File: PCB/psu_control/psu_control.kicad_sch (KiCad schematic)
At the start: 7 parts, among them Q1 SSM3J372R, U1 LM810M3-4.63, U2 Teensy_LC

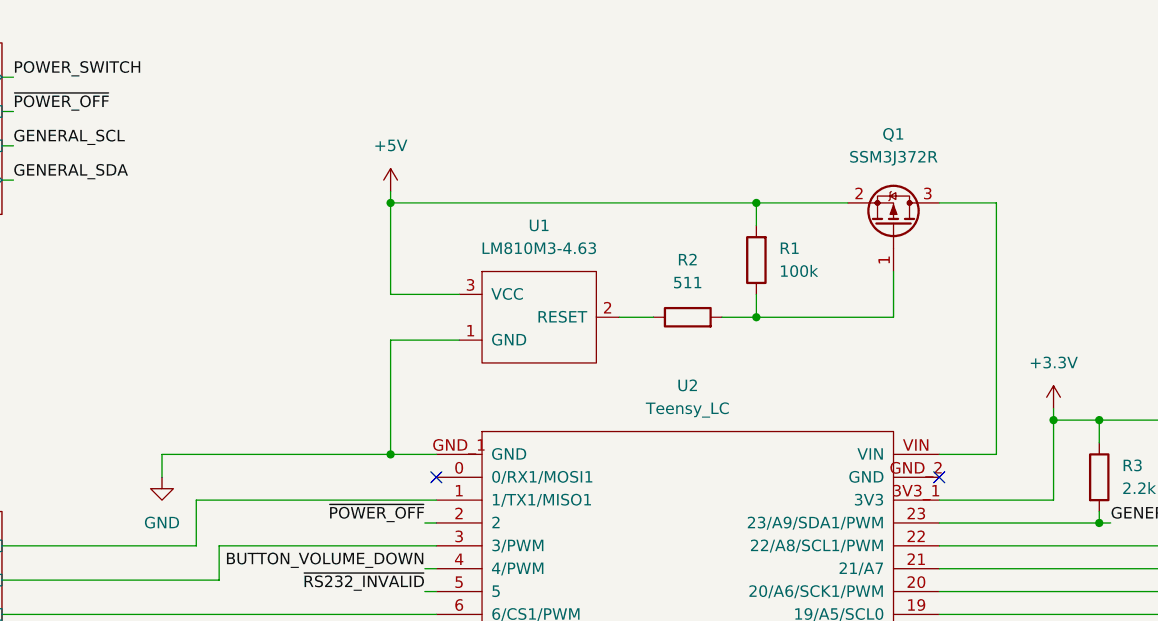
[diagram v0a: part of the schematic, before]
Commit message: Remove voltage supervisors
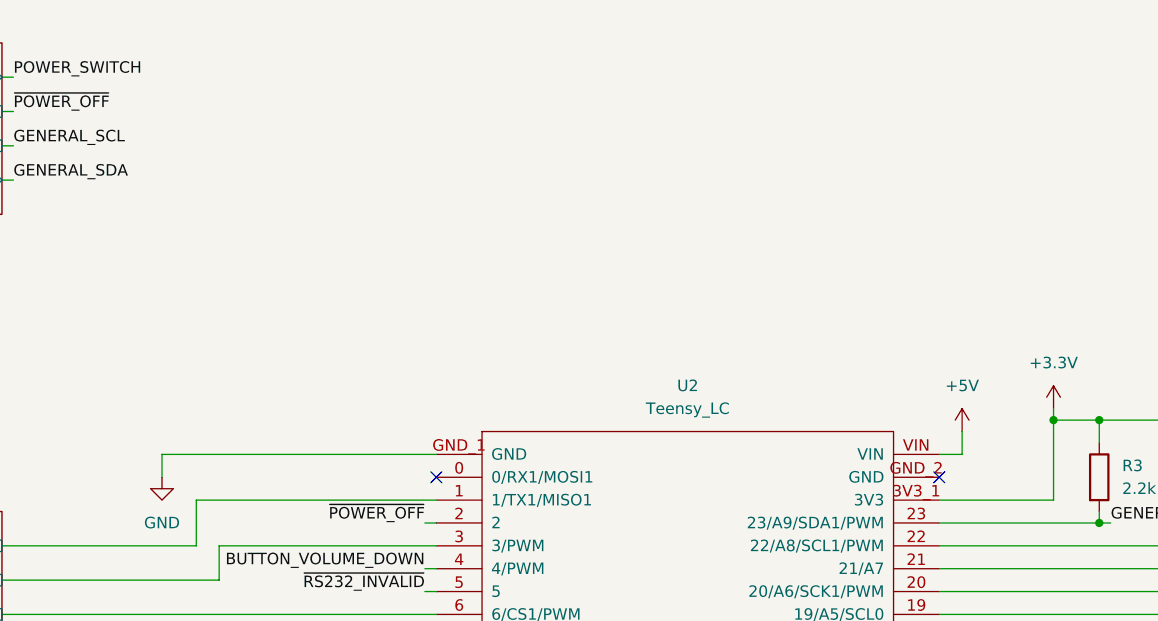
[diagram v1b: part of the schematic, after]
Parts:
- removed Q1: SSM3J372R, Package_TO_SOT_SMD:SOT-23, symbol Device:Q_PMOS_GSD
- removed R1: 100k, Resistor_SMD:R_0805_2012Metric, symbol Device:R
- removed R2: 511, Resistor_SMD:R_0805_2012Metric, symbol Device:R
- removed U1: LM810M3-4.63, Package_TO_SOT_SMD:SOT-23, symbol t-top:LM810
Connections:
- net +5V: now also U2.VIN
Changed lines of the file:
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@@
   (junction (at 168.91 69.85) (diameter 0) (color 0 0 0 0)
   )
-  (junction (at 95.25 45.72) (diameter 0) (color 0 0 0 0)
-  )
-  (junction (at 135.89 45.72) (diameter 0) (color 0 0 0 0)
-  )
-  (junction (at 95.25 73.66) (diameter 0) (color 0 0 0 0)
-  )
   (junction (at 190.5 83.82) (diameter 0) (color 0 0 0 0)
-  )
-  (junction (at 135.89 58.42) (diameter 0) (color 0 0 0 0)
   )
   (junction (at 173.99 69.85) (diameter 0) (color 0 0 0 0)
@@
     (stroke (width 0) (type default) (color 0 0 0 0))
   )
-  (wire (pts (xy 162.56 73.66) (xy 156.21 73.66))
-    (stroke (width 0) (type default) (color 0 0 0 0))
-  )
   (wire (pts (xy 74.93 96.52) (xy 74.93 118.11))
     (stroke (width 0) (type default) (color 0 0 0 0))
@@
     (stroke (width 0) (type default) (color 0 0 0 0))
   )
-  (wire (pts (xy 120.65 58.42) (xy 124.46 58.42))
-    (stroke (width 0) (type default) (color 0 0 0 0))
-  )
-  (wire (pts (xy 95.25 60.96) (xy 95.25 73.66))
-    (stroke (width 0) (type default) (color 0 0 0 0))
-  )
-  (wire (pts (xy 135.89 58.42) (xy 135.89 55.88))
-    (stroke (width 0) (type default) (color 0 0 0 0))
-  )
   (wire (pts (xy 168.91 68.58) (xy 168.91 69.85))
     (stroke (width 0) (type default) (color 0 0 0 0))
   )
+  (wire (pts (xy 158.75 71.12) (xy 158.75 73.66))
+    (stroke (width 0) (type default) (color 0 0 0 0))
+  )
   (wire (pts (xy 212.09 147.32) (xy 213.36 147.32))
     (stroke (width 0) (type default) (color 0 0 0 0))
@@
     (stroke (width 0) (type default) (color 0 0 0 0))
   )
-  (wire (pts (xy 95.25 55.88) (xy 102.87 55.88))
-    (stroke (width 0) (type default) (color 0 0 0 0))
-  )
   (wire (pts (xy 156.21 78.74) (xy 168.91 78.74))
     (stroke (width 0) (type default) (color 0 0 0 0))
@@
     (stroke (width 0) (type default) (color 0 0 0 0))
   )
-  (wire (pts (xy 135.89 45.72) (xy 135.89 48.26))
+  (wire (pts (xy 158.75 73.66) (xy 156.21 73.66))
     (stroke (width 0) (type default) (color 0 0 0 0))
   )
@@
     (stroke (width 0) (type default) (color 0 0 0 0))
   )
-  (wire (pts (xy 151.13 53.34) (xy 151.13 58.42))
-    (stroke (width 0) (type default) (color 0 0 0 0))
-  )
   (wire (pts (xy 156.21 91.44) (xy 210.82 91.44))
     (stroke (width 0) (type default) (color 0 0 0 0))
@@
     (stroke (width 0) (type default) (color 0 0 0 0))
   )
-  (wire (pts (xy 100.33 73.66) (xy 95.25 73.66))
-    (stroke (width 0) (type default) (color 0 0 0 0))
-  )
   (wire (pts (xy 185.42 129.54) (xy 185.42 104.14))
     (stroke (width 0) (type default) (color 0 0 0 0))
@@
     (stroke (width 0) (type default) (color 0 0 0 0))
   )
-  (wire (pts (xy 135.89 45.72) (xy 146.05 45.72))
-    (stroke (width 0) (type default) (color 0 0 0 0))
-  )
   (wire (pts (xy 190.5 69.85) (xy 190.5 72.39))
     (stroke (width 0) (type default) (color 0 0 0 0))
   )
-  (wire (pts (xy 132.08 58.42) (xy 135.89 58.42))
-    (stroke (width 0) (type default) (color 0 0 0 0))
-  )
   (wire (pts (xy 212.09 143.51) (xy 213.36 143.51))
     (stroke (width 0) (type default) (color 0 0 0 0))
   )
-  (wire (pts (xy 95.25 45.72) (xy 95.25 55.88))
-    (stroke (width 0) (type default) (color 0 0 0 0))
-  )
   (wire (pts (xy 156.21 101.6) (xy 186.69 101.6))
     (stroke (width 0) (type default) (color 0 0 0 0))
@@
     (stroke (width 0) (type default) (color 0 0 0 0))
   )
-  (wire (pts (xy 162.56 45.72) (xy 162.56 73.66))
-    (stroke (width 0) (type default) (color 0 0 0 0))
-  )
   (wire (pts (xy 99.06 99.06) (xy 100.33 99.06))
     (stroke (width 0) (type default) (color 0 0 0 0))
   )
-  (wire (pts (xy 69.85 73.66) (xy 95.25 73.66))
+  (wire (pts (xy 69.85 73.66) (xy 100.33 73.66))
     (stroke (width 0) (type default) (color 0 0 0 0))
   )
@@
     (stroke (width 0) (type default) (color 0 0 0 0))
   )
-  (wire (pts (xy 95.25 45.72) (xy 135.89 45.72))
-    (stroke (width 0) (type default) (color 0 0 0 0))
-  )
   (wire (pts (xy 156.21 96.52) (xy 189.23 96.52))
     (stroke (width 0) (type default) (color 0 0 0 0))
   )
-  (wire (pts (xy 151.13 58.42) (xy 135.89 58.42))
-    (stroke (width 0) (type default) (color 0 0 0 0))
-  )
   (wire (pts (xy 52.07 121.92) (xy 53.34 121.92))
     (stroke (width 0) (type default) (color 0 0 0 0))
@@
     (stroke (width 0) (type default) (color 0 0 0 0))
   )
-  (wire (pts (xy 156.21 45.72) (xy 162.56 45.72))
-    (stroke (width 0) (type default) (color 0 0 0 0))
-  )
   (wire (pts (xy 212.09 111.76) (xy 213.36 111.76))
     (stroke (width 0) (type default) (color 0 0 0 0))
@@
     (stroke (width 0) (type default) (color 0 0 0 0))
   )
-  (wire (pts (xy 95.25 44.45) (xy 95.25 45.72))
-    (stroke (width 0) (type default) (color 0 0 0 0))
-  )
   (wire (pts (xy 74.93 118.11) (xy 52.07 118.11))
     (stroke (width 0) (type default) (color 0 0 0 0))
@@
   )
   (wire (pts (xy 76.2 83.82) (xy 100.33 83.82))
-    (stroke (width 0) (type default) (color 0 0 0 0))
-  )
-  (wire (pts (xy 102.87 60.96) (xy 95.25 60.96))
     (stroke (width 0) (type default) (color 0 0 0 0))
   )
@@
     (pin "1")
   )
-  (symbol (lib_id "t-top:LM810") (at 111.76 52.07 0) (unit 1)
+  (symbol (lib_id "power:+5V") (at 158.75 71.12 0) (unit 1)
     (in_bom yes) (on_board yes) (fields_autoplaced)
-    (property "Reference" "U1" (id 0) (at 111.76 48.26 0))
-    (property "Value" "LM810M3-4.63" (id 1) (at 111.76 50.8 0))
-    (property "Footprint" "Package_TO_SOT_SMD:SOT-23" (id 2) (at 111.76 52.07 0)
-      (effects (font (size 1.27 1.27)) hide)
-    )
-    (property "Datasheet" "" (id 3) (at 111.76 52.07 0)
-      (effects (font (size 1.27 1.27)) hide)
-    )
-    (pin "1")
-    (pin "2")
-    (pin "3")
-  )
-  (symbol (lib_id "Device:Q_PMOS_GSD") (at 151.13 48.26 270) (mirror x) (unit 1)
-    (in_bom yes) (on_board yes) (fields_autoplaced)
-    (property "Reference" "Q1" (id 0) (at 151.13 38.1 90))
-    (property "Value" "SSM3J372R" (id 1) (at 151.13 40.64 90))
-    (property "Footprint" "Package_TO_SOT_SMD:SOT-23" (id 2) (at 153.67 43.18 0)
-      (effects (font (size 1.27 1.27)) hide)
-    )
-    (property "Datasheet" "~" (id 3) (at 151.13 48.26 0)
-      (effects (font (size 1.27 1.27)) hide)
-    )
-    (pin "1")
-    (pin "2")
-    (pin "3")
-  )
-  (symbol (lib_id "Device:R") (at 135.89 52.07 180) (unit 1)
-    (in_bom yes) (on_board yes) (fields_autoplaced)
-    (property "Reference" "R1" (id 0) (at 138.43 50.7999 0)
-      (effects (font (size 1.27 1.27)) (justify right))
-    )
-    (property "Value" "100k" (id 1) (at 138.43 53.3399 0)
-      (effects (font (size 1.27 1.27)) (justify right))
-    )
-    (property "Footprint" "Resistor_SMD:R_0805_2012Metric" (id 2) (at 137.668 52.07 90)
-      (effects (font (size 1.27 1.27)) hide)
-    )
-    (property "Datasheet" "~" (id 3) (at 135.89 52.07 0)
-      (effects (font (size 1.27 1.27)) hide)
-    )
-    (pin "1")
-    (pin "2")
-  )
-  (symbol (lib_id "power:+5V") (at 95.25 44.45 0) (unit 1)
-    (in_bom yes) (on_board yes) (fields_autoplaced)
-    (property "Reference" "#PWR0103" (id 0) (at 95.25 48.26 0)
-      (effects (font (size 1.27 1.27)) hide)
-    )
-    (property "Value" "+5V" (id 1) (at 95.25 39.37 0))
-    (property "Footprint" "" (id 2) (at 95.25 44.45 0)
-      (effects (font (size 1.27 1.27)) hide)
-    )
-    (property "Datasheet" "" (id 3) (at 95.25 44.45 0)
+    (property "Reference" "#PWR0103" (id 0) (at 158.75 74.93 0)
+      (effects (font (size 1.27 1.27)) hide)
+    )
+    (property "Value" "+5V" (id 1) (at 158.75 66.04 0))
+    (property "Footprint" "" (id 2) (at 158.75 71.12 0)
+      (effects (font (size 1.27 1.27)) hide)
+    )
+    (property "Datasheet" "" (id 3) (at 158.75 71.12 0)
       (effects (font (size 1.27 1.27)) hide)
     )
@@
     (pin "2")
   )
-  (symbol (lib_id "Device:R") (at 128.27 58.42 90) (unit 1)
-    (in_bom yes) (on_board yes) (fields_autoplaced)
-    (property "Reference" "R2" (id 0) (at 128.27 52.07 90))
-    (property "Value" "511" (id 1) (at 128.27 54.61 90))
-    (property "Footprint" "Resistor_SMD:R_0805_2012Metric" (id 2) (at 128.27 60.198 90)
-      (effects (font (size 1.27 1.27)) hide)
-    )
-    (property "Datasheet" "~" (id 3) (at 128.27 58.42 0)
-      (effects (font (size 1.27 1.27)) hide)
-    )
-    (pin "1")
-    (pin "2")
-  )
   (sheet (at 25.4 27.94) (size 26.67 19.05) (fields_autoplaced)
     (stroke (width 0.1524) (type solid) (color 0 0 0 0))
@@
       (reference "M2") (unit 1) (value "Fan") (footprint "Connector_JST:JST_PH_B2B-PH-K_1x02_P2.00mm_Vertical")
     )
-    (path "/681258c1-f3a6-4fab-a15e-0535fb91fd3d"
-      (reference "Q1") (unit 1) (value "SSM3J372R") (footprint "Package_TO_SOT_SMD:SOT-23")
-    )
     (path "/0ec1e19c-2d8a-40fb-a27f-fde467b9d0d4/0809d4d3-1d96-45bd-90ca-260d8d265f6b"
       (reference "Q2") (unit 1) (value "IPD068P03L3GATMA1") (footprint "Package_TO_SOT_SMD:TO-252-2")
@@
       (reference "Q4") (unit 2) (value "DMG9926USD") (footprint "Package_SO:SOIC-8_3.9x4.9mm_P1.27mm")
     )
-    (path "/7ab13c23-9ab9-4388-814f-caf1cd546214"
-      (reference "R1") (unit 1) (value "100k") (footprint "Resistor_SMD:R_0805_2012Metric")
-    )
-    (path "/d4a91fd7-5ca6-4aef-8449-af691df1ee09"
-      (reference "R2") (unit 1) (value "511") (footprint "Resistor_SMD:R_0805_2012Metric")
-    )
     (path "/8dcddcfa-221a-4da6-938c-a371f93d8886"
       (reference "R3") (unit 1) (value "2.2k") (footprint "Resistor_SMD:R_0805_2012Metric")
@@
       (reference "TH2") (unit 1) (value "10k") (footprint "Resistor_SMD:R_0805_2012Metric")
     )
-    (path "/4e86ebe6-ad98-4694-9490-6b15595099ee"
-      (reference "U1") (unit 1) (value "LM810M3-4.63") (footprint "Package_TO_SOT_SMD:SOT-23")
-    )
     (path "/7ff96aac-5e45-4f30-8190-399472c33a05"
